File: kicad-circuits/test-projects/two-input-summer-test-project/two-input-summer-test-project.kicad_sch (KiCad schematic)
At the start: 4 parts

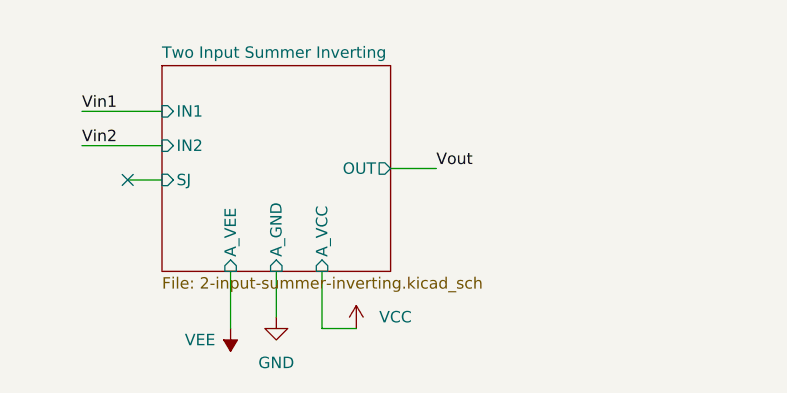
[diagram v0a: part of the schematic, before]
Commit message: Reorganized circuits.
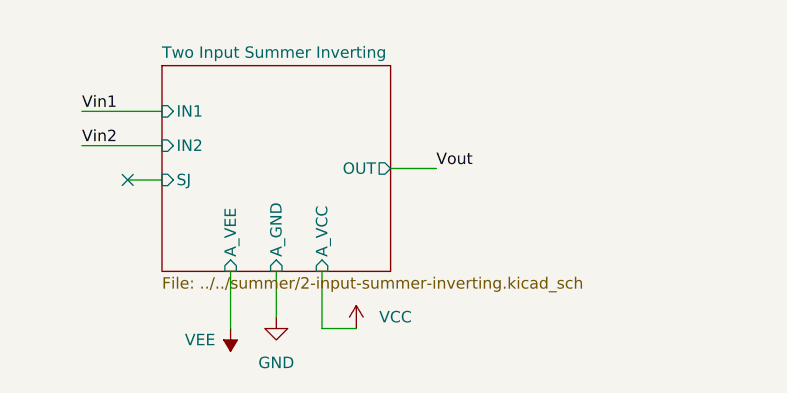
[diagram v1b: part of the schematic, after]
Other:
- sheet Two Input Summer Inverting: file 2-input-summer-inverting.kicad_sch -> ../../summer/2-input-summer-inverting.kicad_sch
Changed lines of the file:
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@@
       (effects (font (size 1.27 1.27)) (justify left bottom))
     )
-    (property "Sheet file" "2-input-summer-inverting.kicad_sch" (id 1) (at 130.81 114.8846 0)
+    (property "Sheet file" "../../summer/2-input-summer-inverting.kicad_sch" (id 1) (at 130.81 114.8846 0)
       (effects (font (size 1.27 1.27)) (justify left top))
     )
